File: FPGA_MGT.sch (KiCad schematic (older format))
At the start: 51 parts, among them J2 HIROSE_U.FL-R-SMT-1(10), J5 HIROSE_U.FL-R-SMT-1(10), U1 XC7K160T-FFG676

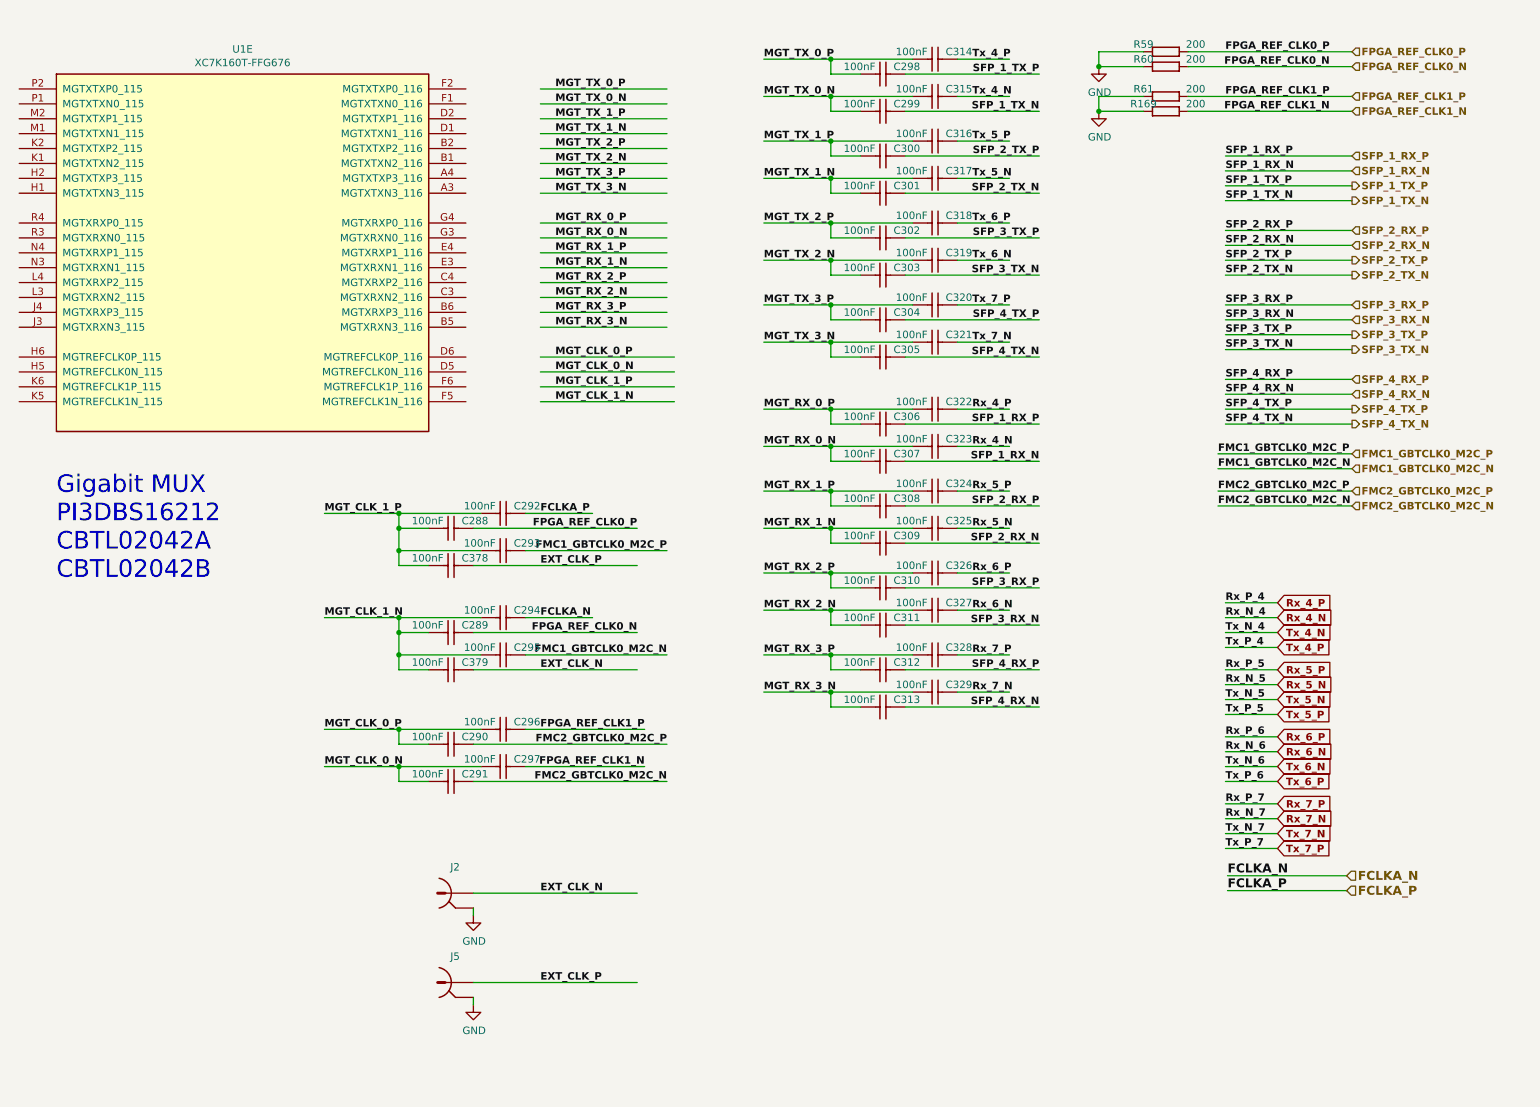
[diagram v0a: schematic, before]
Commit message: MGT mux and QSFP added to the schematics,
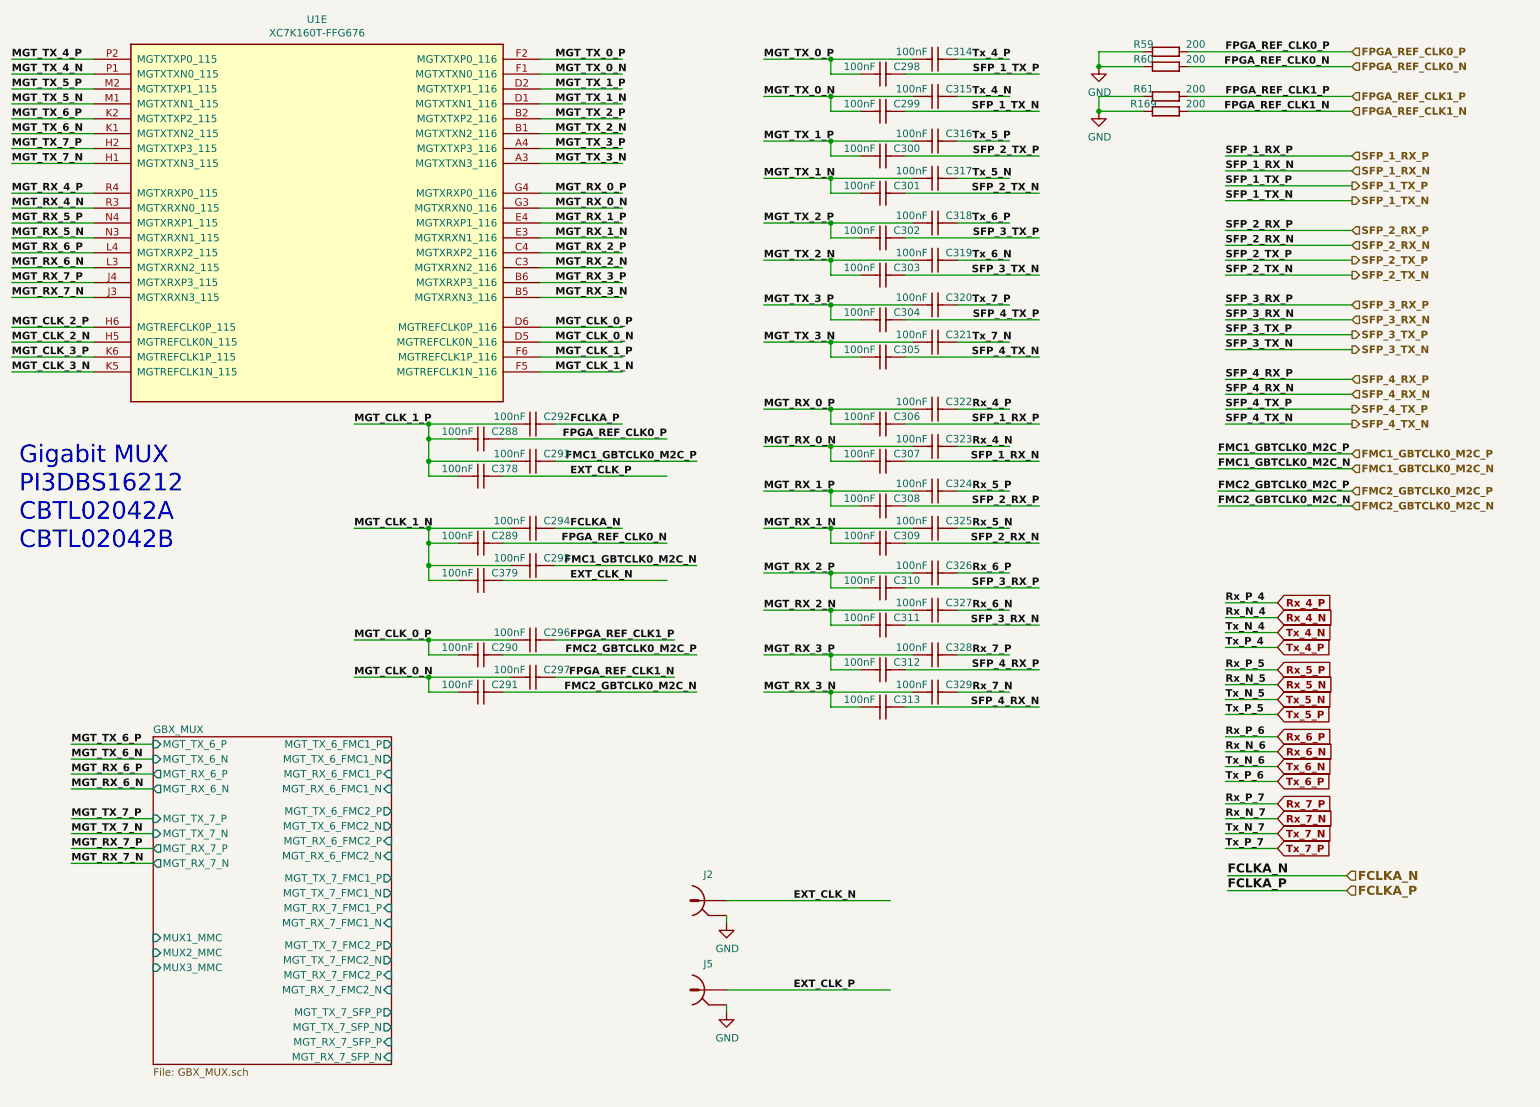
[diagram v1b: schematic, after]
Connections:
- net labels added: MGT_CLK_2_N, MGT_CLK_2_P, MGT_CLK_3_N, MGT_CLK_3_P, MGT_RX_4_N, MGT_RX_4_P, MGT_RX_5_N, MGT_RX_5_P, MGT_RX_6_N, MGT_RX_6_P, MGT_RX_7_N, MGT_RX_7_P, MGT_TX_4_N, MGT_TX_4_P, MGT_TX_5_N, MGT_TX_5_P, MGT_TX_6_N, MGT_TX_6_P, MGT_TX_7_N, MGT_TX_7_P
- wire segments 204 -> 232
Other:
- moved on the sheet: C288, C289, C290, C291, C292, C293, C294, C295, C296, C297, C378, C379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

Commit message: FMC HPC & LPC done, FPGA power delivery done, RGMII lines done,  MGT lines progress
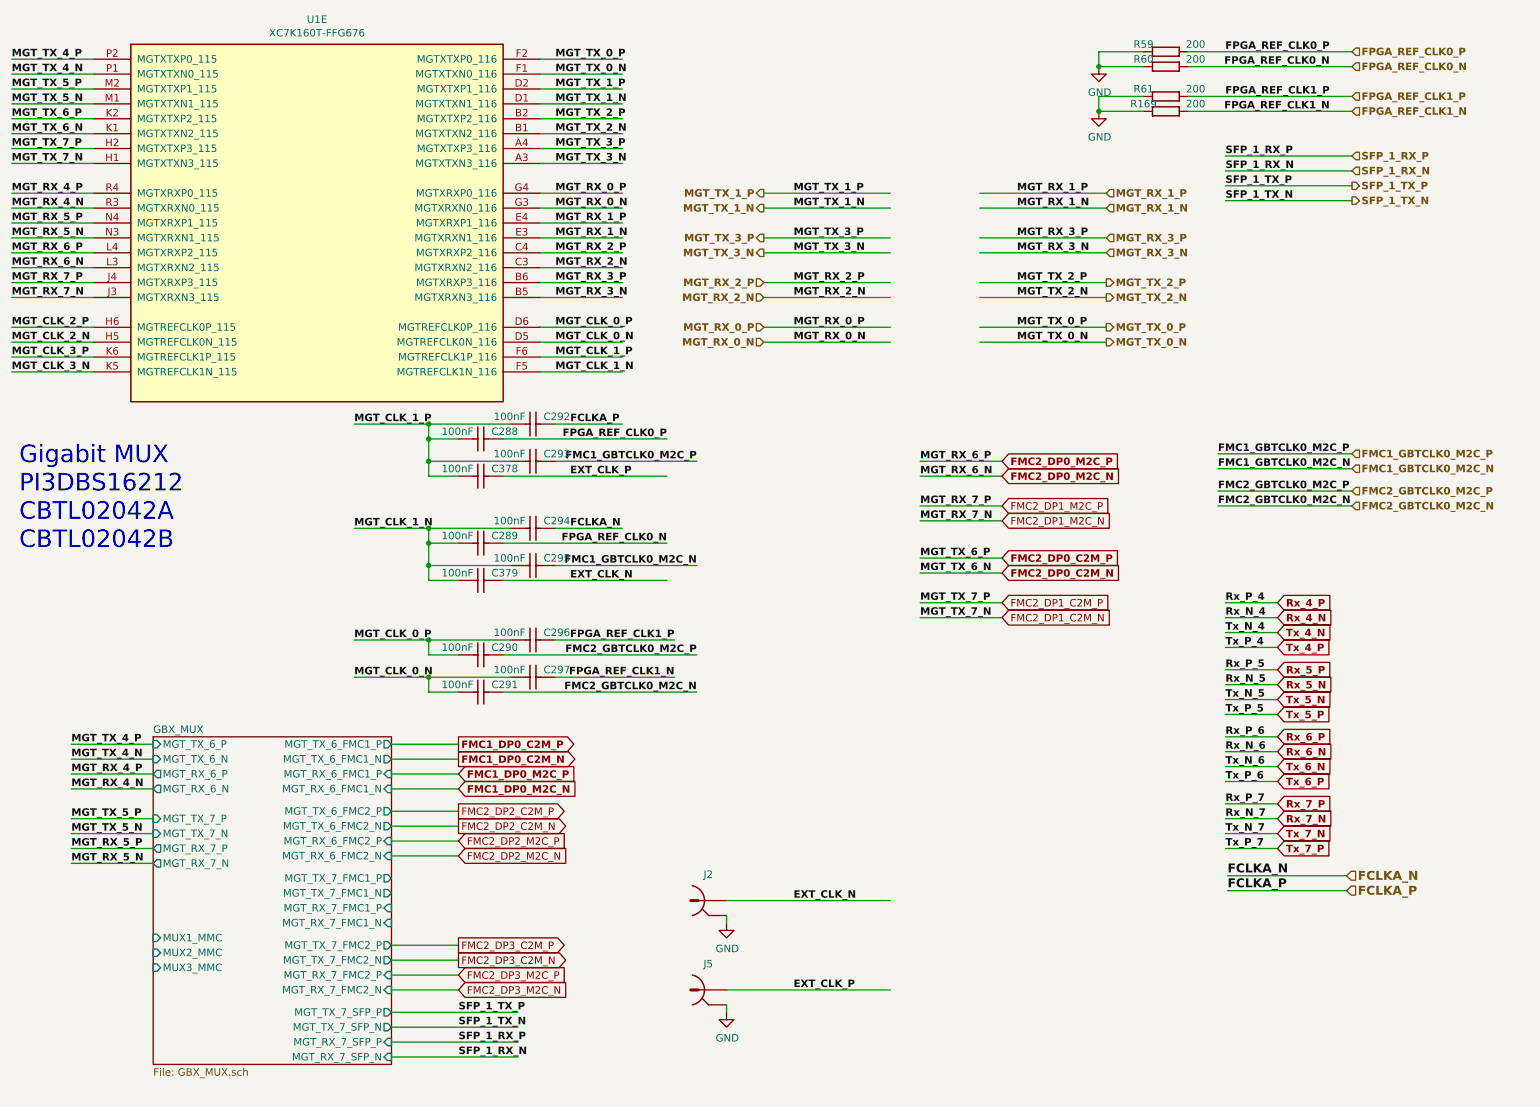
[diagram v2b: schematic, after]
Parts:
- removed C298, C299, C300, C301, C302, C303, C304, C305, C306, C307, C308, C309, C310, C311, C312, C313, C314, C315, C316, C317, C318, C319, C320, C321, C322, C323, C324, C325, C326, C327, C328, C329: CC0201_100NF_6.3V_10%_X5R, CAPC0603X33N, symbol Capacitors_SMD:CC0201_100NF_6.3V_10%_X5R
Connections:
- net labels added: FMC1_DP0_C2M_N, FMC1_DP0_C2M_P, FMC1_DP0_M2C_N, FMC1_DP0_M2C_P, FMC2_DP0_C2M_N, FMC2_DP0_C2M_P, FMC2_DP0_M2C_N, FMC2_DP0_M2C_P, FMC2_DP1_C2M_N, FMC2_DP1_C2M_P, FMC2_DP1_M2C_N, FMC2_DP1_M2C_P, FMC2_DP2_C2M_N, FMC2_DP2_C2M_P, FMC2_DP2_M2C_N, FMC2_DP2_M2C_P, FMC2_DP3_C2M_N, FMC2_DP3_C2M_P, FMC2_DP3_M2C_N, FMC2_DP3_M2C_P
- net labels removed: SFP_2_RX_N, SFP_2_RX_P, SFP_2_TX_N, SFP_2_TX_P, SFP_3_RX_N, SFP_3_RX_P, SFP_3_TX_N, SFP_3_TX_P, SFP_4_RX_N, SFP_4_RX_P, SFP_4_TX_N, SFP_4_TX_P
- wire segments 232 -> 164

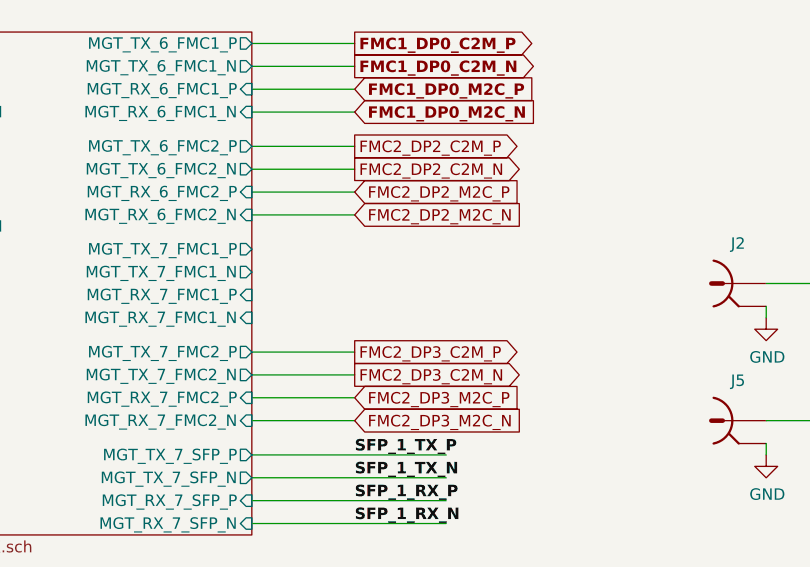
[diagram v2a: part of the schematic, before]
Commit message: FPGA power finished, significant progress on PCB
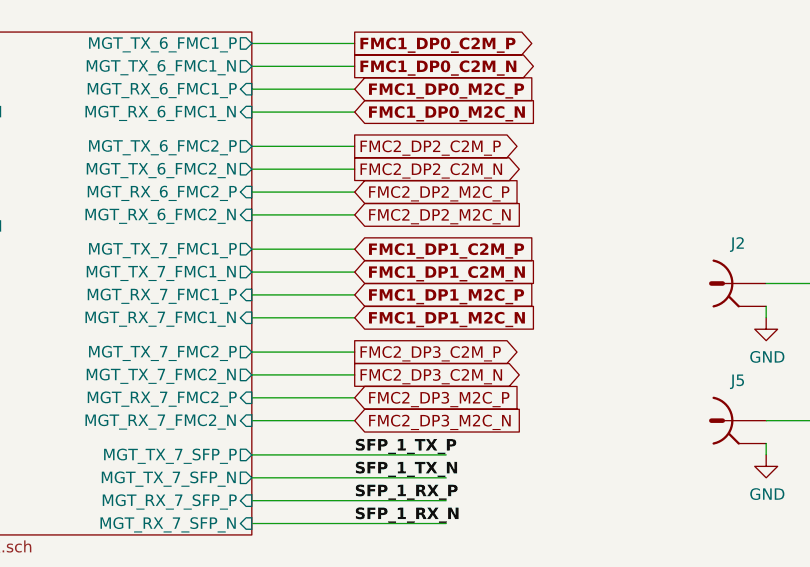
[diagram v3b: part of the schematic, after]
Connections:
- net labels added: FMC1_DP1_C2M_N, FMC1_DP1_C2M_P, FMC1_DP1_M2C_N, FMC1_DP1_M2C_P
- wire segments 164 -> 168
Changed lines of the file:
@@
 $Descr A4 11693 8268
 encoding utf-8
-Sheet 24 25
+Sheet 23 25
 Title "Marble"
 Date "2019-01-16"
@@
 Wire Wire Line
 	3250 7350 4100 7350
+Text GLabel 3700 6350 2    50   Input ~ 10
+FMC1_DP1_C2M_P
+Text GLabel 3700 6450 2    50   Input ~ 10
+FMC1_DP1_C2M_N
+Text GLabel 3700 6550 2    50   Input ~ 10
+FMC1_DP1_M2C_P
+Text GLabel 3700 6650 2    50   Input ~ 10
+FMC1_DP1_M2C_N
+Wire Wire Line
+	3250 6350 3700 6350
+Wire Wire Line
+	3250 6450 3700 6450
+Wire Wire Line
+	3250 6550 3700 6550
+Wire Wire Line
+	3250 6650 3700 6650
 $EndSCHEMATC

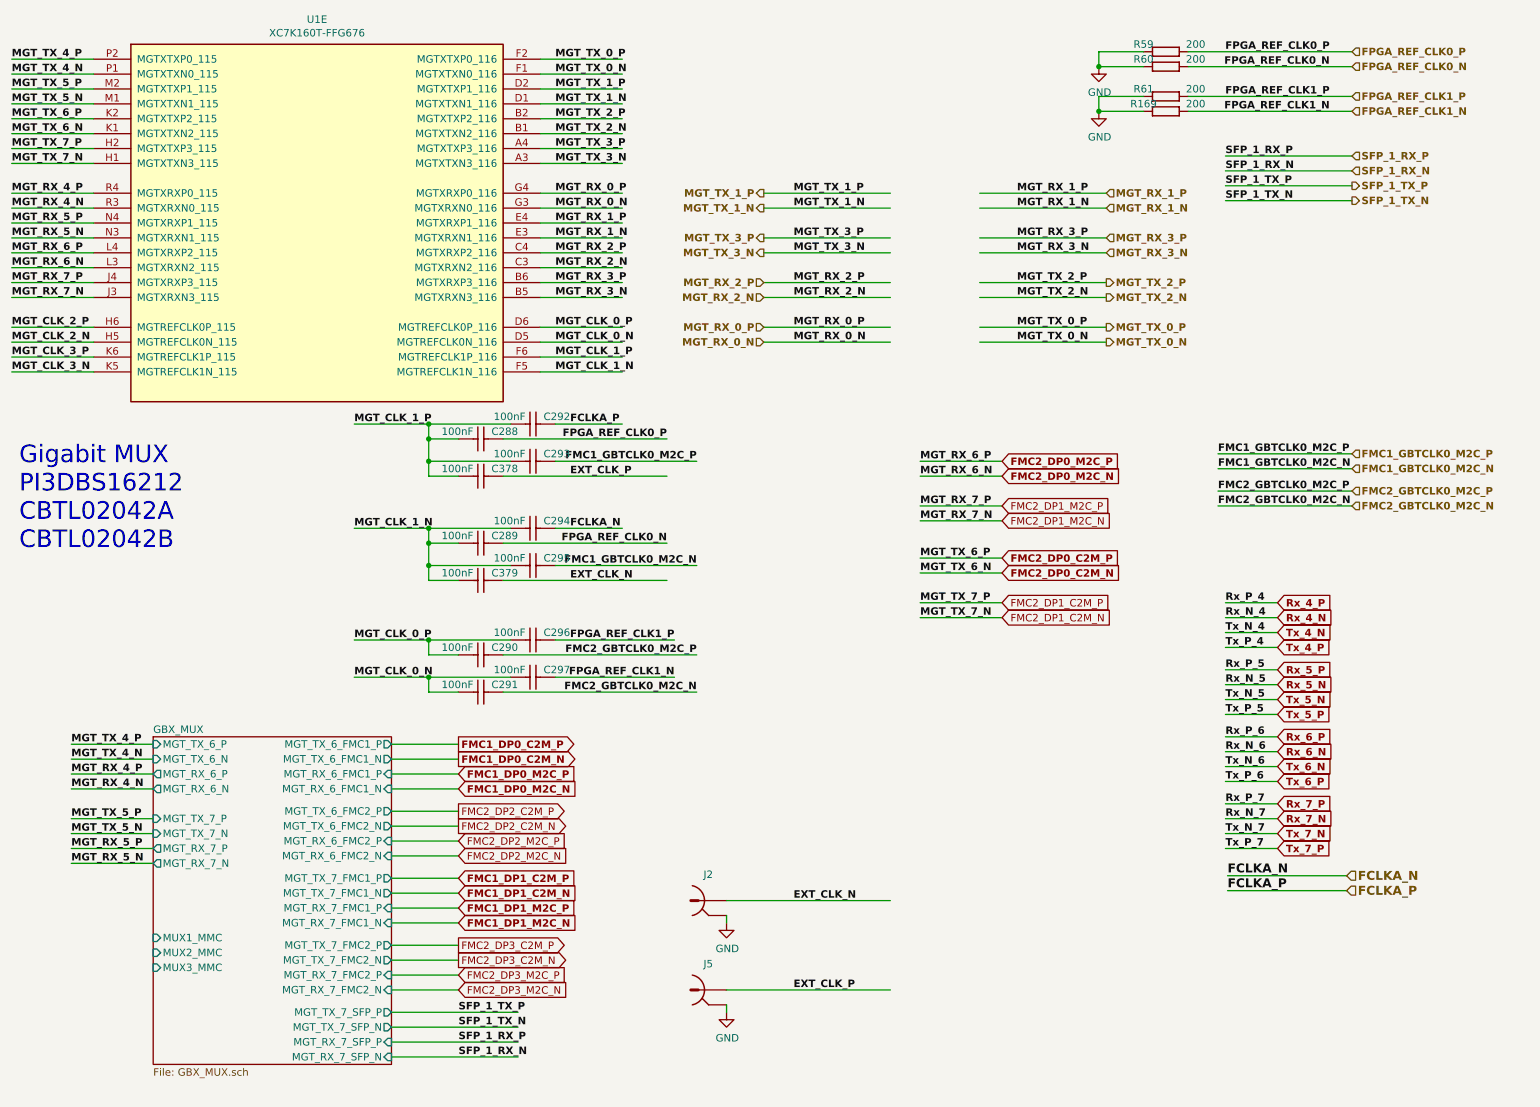
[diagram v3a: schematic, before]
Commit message: new board outline, rearranging banks connections, SODIMM memory
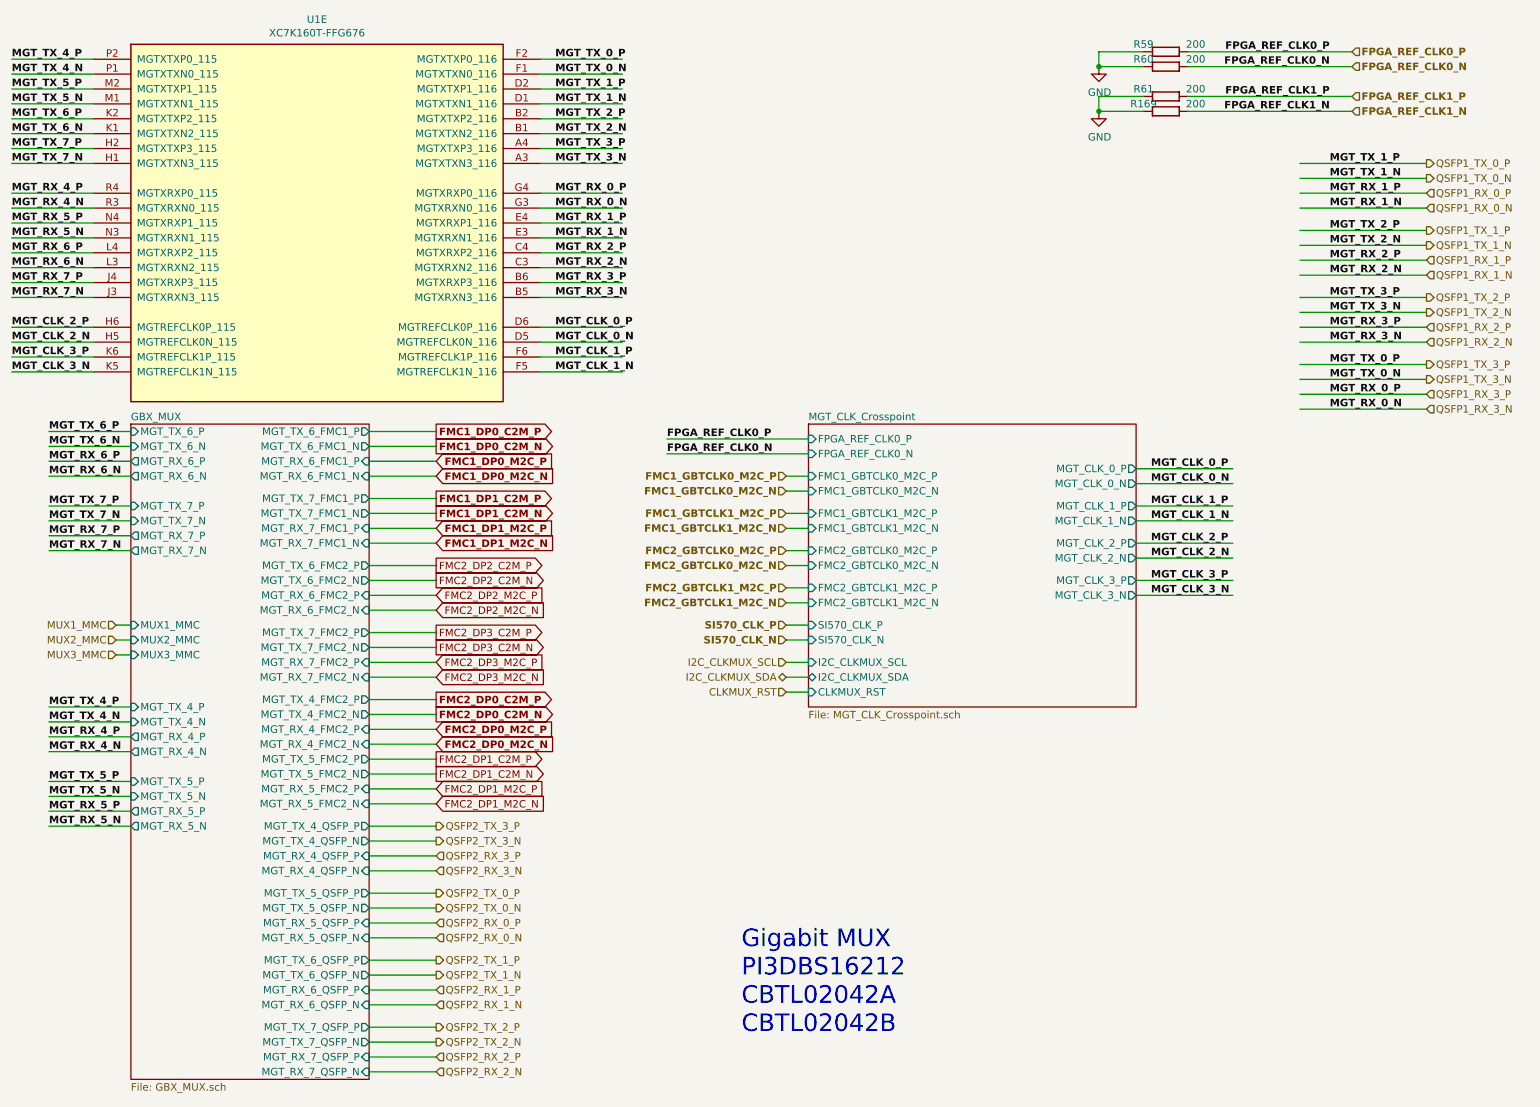
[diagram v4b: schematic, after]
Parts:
- removed C288, C289, C290, C291, C292, C293, C294, C295, C296, C297, C378, C379: CC0201_100NF_6.3V_10%_X5R, CAPC0603X33N, symbol Capacitors_SMD:CC0201_100NF_6.3V_10%_X5R
- removed J2, J5: HIROSE_U.FL-R-SMT-1(10), AG5300_2:U.FL_Hirose_U.FL-R-SMT-1_Vertical, symbol Miscellaneous:HIROSE_U.FL-R-SMT-1(10)
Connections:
- net labels added: CLKMUX_RST, FMC1_GBTCLK1_M2C_N, FMC1_GBTCLK1_M2C_P, FMC2_GBTCLK1_M2C_N, FMC2_GBTCLK1_M2C_P, I2C_CLKMUX_SCL, I2C_CLKMUX_SDA, MUX1_MMC, MUX2_MMC, MUX3_MMC, QSFP1_RX_0_N, QSFP1_RX_0_P, QSFP1_RX_1_N, QSFP1_RX_1_P, QSFP1_RX_2_N, QSFP1_RX_2_P, QSFP1_RX_3_N, QSFP1_RX_3_P, QSFP1_TX_0_N, QSFP1_TX_0_P, QSFP1_TX_1_N, QSFP1_TX_1_P, QSFP1_TX_2_N, QSFP1_TX_2_P, QSFP1_TX_3_N, QSFP1_TX_3_P, QSFP2_RX_0_N, QSFP2_RX_0_P, QSFP2_RX_1_N, QSFP2_RX_1_P, QSFP2_RX_2_N, QSFP2_RX_2_P, QSFP2_RX_3_N, QSFP2_RX_3_P, QSFP2_TX_0_N, QSFP2_TX_0_P, QSFP2_TX_1_N, QSFP2_TX_1_P, QSFP2_TX_2_N, QSFP2_TX_2_P, QSFP2_TX_3_N, QSFP2_TX_3_P, SI570_CLK_N, SI570_CLK_P
- net labels removed: EXT_CLK_N, EXT_CLK_P, FCLKA_N, FCLKA_P, Rx_4_N, Rx_4_P, Rx_5_N, Rx_5_P, Rx_6_N, Rx_6_P, Rx_7_N, Rx_7_P, Rx_N_4, Rx_N_5, Rx_N_6, Rx_N_7, Rx_P_4, Rx_P_5, Rx_P_6, Rx_P_7, SFP_1_RX_N, SFP_1_RX_P, SFP_1_TX_N, SFP_1_TX_P, Tx_4_N, Tx_4_P, Tx_5_N, Tx_5_P, Tx_6_N, Tx_6_P, Tx_7_N, Tx_7_P, Tx_N_4, Tx_N_5, Tx_N_6, Tx_N_7, Tx_P_4, Tx_P_5, Tx_P_6, Tx_P_7
- wire segments 168 -> 148
